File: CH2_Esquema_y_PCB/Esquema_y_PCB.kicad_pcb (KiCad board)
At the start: 2 copper layers, 230 x 106.5 mm, 44 parts, among them Q1 BC547, Q10 BC857, Q2 BC547, Q3 BC547, Q4 BC547, Q5 IRF9Z34N, Q7 BC547, Q9 BC857, U1 TL431LP, U2 LM358

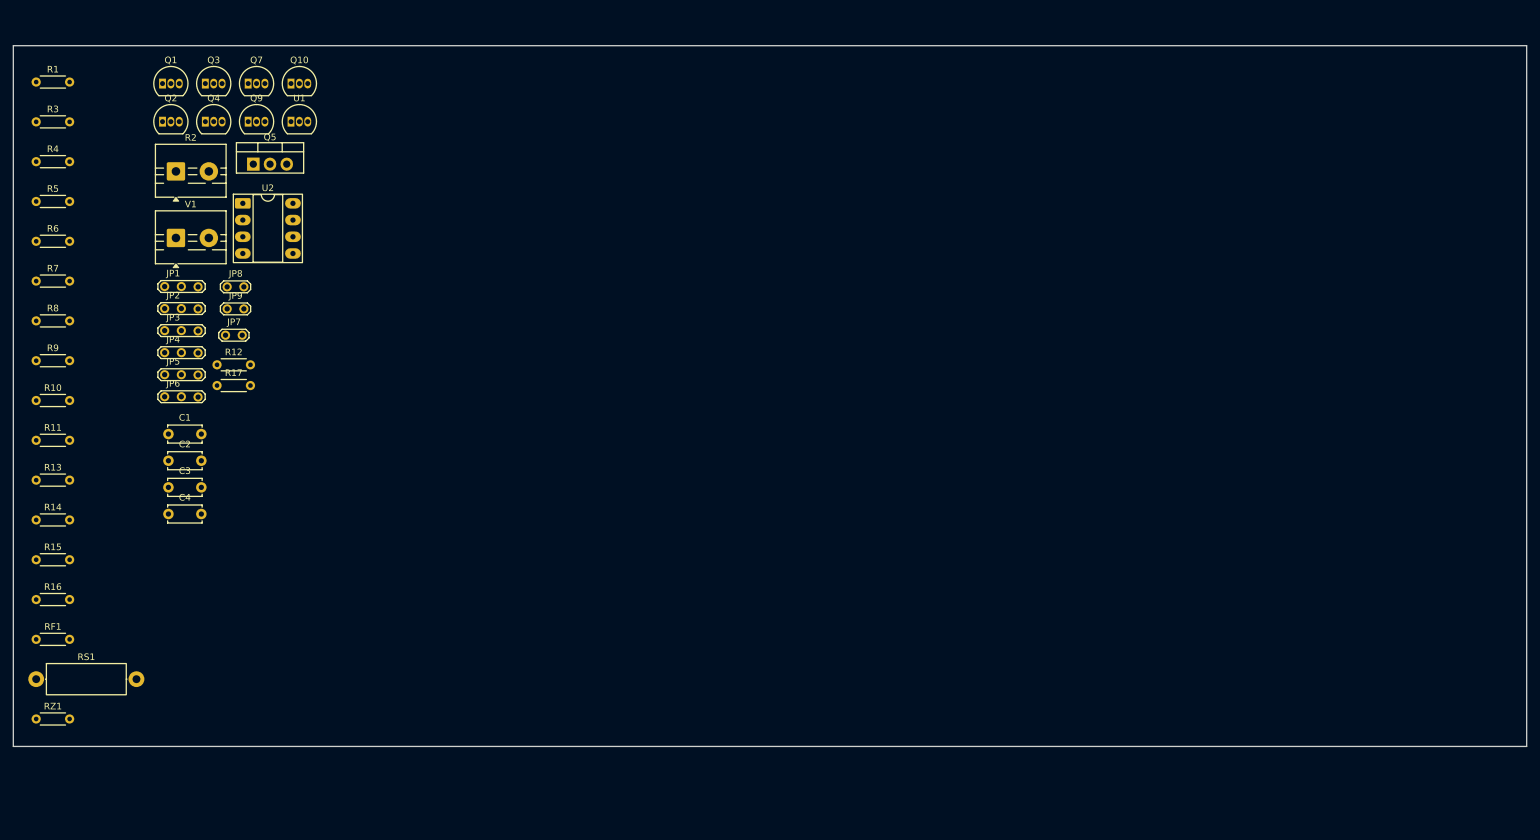
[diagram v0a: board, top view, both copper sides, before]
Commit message: PCB para impresion. Se modifican Jumpers en esquematico
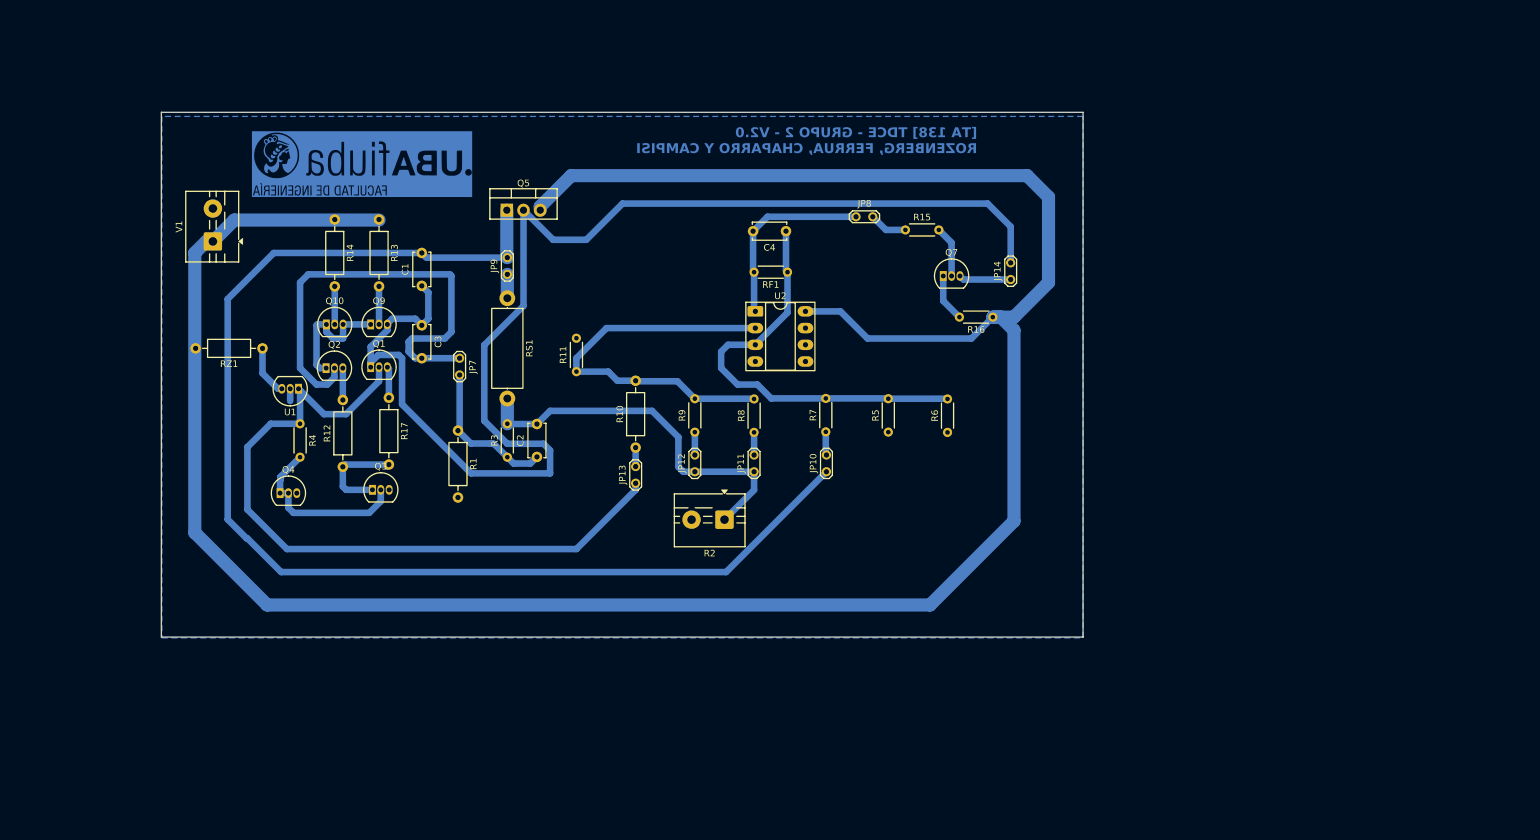
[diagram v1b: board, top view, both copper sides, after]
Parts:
- removed JP1, JP2, JP3, JP4, JP5, JP6: Jumper_3_Bridged12, Jumper_triple:TestPoint_2Pads_Pitch2.54mm_Drill0.8mm
- added G***: LOGO, LOGO, B.Cu at (77.5, 43.0)
- added JP10: Jumper_2_Bridged, TestPoint:TestPoint_2Pads_Pitch2.54mm_Drill0.8mm, F.Cu at (148.1, 89.8)
- added JP11: Jumper_2_Bridged, TestPoint:TestPoint_2Pads_Pitch2.54mm_Drill0.8mm, F.Cu at (137.1, 89.8)
- added JP12: Jumper_2_Bridged, TestPoint:TestPoint_2Pads_Pitch2.54mm_Drill0.8mm, F.Cu at (128.1, 89.8)
- added JP13: Jumper_2_Bridged, TestPoint:TestPoint_2Pads_Pitch2.54mm_Drill0.8mm, F.Cu at (119.1, 91.5)
- added JP14: Jumper_2_Bridged, TestPoint:TestPoint_2Pads_Pitch2.54mm_Drill0.8mm, F.Cu at (176.1, 60.5)
- R1, R10, R12, R13, R14, R17, RZ1: footprint Resistor_THT:R_Axial_DIN0204_L3.6mm_D1.6mm_P5.08mm_Horizontal -> Resistor_THT:R_Axial_DIN0207_L6.3mm_D2.5mm_P10.16mm_Horizontal
- moved R16 151.6 mm to (173.4, 66.2), turned to 180 degrees
- moved R6 141.5 mm to (166.5, 83.8), turned to 90 degrees
- moved R15 141.3 mm to (160.1, 53.0)
- moved R5 134.2 mm to (157.5, 83.7), turned to 90 degrees
- moved RF1 127.1 mm to (142.2, 59.4), turned to 180 degrees
- moved R7 122.2 mm to (148.0, 83.7), turned to 90 degrees
- moved R8 110.4 mm to (137.1, 83.8), turned to 90 degrees
- moved Q7 109.6 mm to (165.8, 60.0)
- moved C4 103.2 mm to (141.9, 53.2), turned to 180 degrees
- moved R9 100.7 mm to (128.1, 83.7), turned to 90 degrees
- moved R2 98.7 mm to (132.6, 97.0), turned to 180 degrees
- moved JP8 96.2 mm to (152.6, 51.0)
- moved RS1 92.1 mm to (99.6, 63.4), turned to -90 degrees
- moved R10 91.4 mm to (119.1, 86.1), turned to 90 degrees
- moved R3 87.9 mm to (99.6, 87.5), turned to 90 degrees
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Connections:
- Q7 pad 3: /gate -> Net-(JP14-A)
- R5 pad 1: Net-(JP1-C) -> GND
- R6 pad 1: Net-(JP2-C) -> GND
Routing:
- net VCC: track 0.00 -> 376.3 mm
- net /gate: track 0.00 -> 195.6 mm
- net /drain: track 0.00 -> 187.1 mm
- net /in: track 0.00 -> 109.0 mm
- net Net-(JP7-A): track 0.00 -> 70.0 mm
- net Net-(U2A-+): track 0.00 -> 64.1 mm
- net Net-(U2A--): track 0.00 -> 59.9 mm
- net /out: track 0.00 -> 57.8 mm
- net Net-(JP8-A): track 0.00 -> 28.9 mm
- net Net-(Q3-B): track 0.00 -> 27.1 mm
- net Net-(JP7-B): track 0.00 -> 23.0 mm
- net Net-(Q10-B): track 0.00 -> 19.6 mm
- net Net-(Q3-C): track 0.00 -> 15.4 mm
- net Net-(JP14-A): track 0.00 -> 7.93 mm
- net Net-(Q7-B): track 0.00 -> 7.80 mm
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- added copper zone on B.Cu, net GND
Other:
- board size 230 x 106.5 mm -> 140.1 x 79.8 mm
- board text added: "[TA 138] TDCE - GRUPO 2 - V2.0 ROZENBERG, FERRUA, CHAPARRO Y CAMPISI"

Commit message: Rehecho PCB
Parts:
- C2, C3: footprint Capacitor_THT:C_Disc_D5.0mm_W2.5mm_P5.00mm -> Capacitor_THT:C_Disc_D7.5mm_W5.0mm_P7.50mm
- Q1, Q10, Q2, Q3, Q4, Q7, Q9, U1: footprint Package_TO_SOT_THT:TO-92_Inline -> Package_TO_SOT_THT:TO-92_Wide
- R11, R15, R16, R3, R4, R5, R6, R7, R8, R9, RF1: footprint Resistor_THT:R_Axial_DIN0204_L3.6mm_D1.6mm_P5.08mm_Horizontal -> Resistor_THT:R_Axial_DIN0207_L6.3mm_D2.5mm_P10.16mm_Horizontal
- RS1: footprint Resistor_THT:R_Axial_DIN0414_L11.9mm_D4.5mm_P15.24mm_Horizontal -> Resistor_THT:R_Axial_Power_L20.0mm_W6.4mm_P25.40mm
- moved G*** 112.4 mm to (169.1, 108.2)
- moved JP10 44.2 mm to (122.1, 54.0), turned to -90 degrees
- moved R16 35.2 mm to (148.0, 41.8), turned to -90 degrees
- moved R7 34.4 mm to (122.1, 61.0), turned to -90 degrees
- moved R11 18.7 mm to (126.5, 65.7)
- moved R6 18.4 mm to (148.8, 89.0)
- moved R5 14.5 mm to (143.9, 88.9)
- moved Q7 14.5 mm to (151.5, 58.3)
- moved V1 14.3 mm to (50.8, 41.0), turned to -90 degrees
- moved RS1 12.6 mm to (109.5, 55.6)
- moved Q10 11.8 mm to (63.7, 59.0), turned to -90 degrees
- moved C3 11.6 mm to (96.5, 61.5)
- moved R15 11.0 mm to (170.5, 49.4), turned to -90 degrees
- moved C2 9.83 mm to (96.8, 80.9), turned to 0 degrees
- moved R1 9.36 mm to (94.2, 92.6)
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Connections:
- Q10 pad 1: Net-(Q10-B) -> Net-(Q10-E)
- Q10 pad 2: Net-(Q10-E) -> Net-(Q10-B)
- Q5 pad 1: /drain -> /gate
- Q5 pad 2: /gate -> /drain
- Q9 pad 1: Net-(Q10-B) -> Net-(Q9-E)
- Q9 pad 2: Net-(Q9-E) -> Net-(Q10-B)
- U2 pad 5: (no net) -> GND
- U2 pad 6: (no net) -> GND
- U2 pad 7: (no net) -> GND
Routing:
- net /drain: track 187.1 -> 55.4 mm
- net /gate: track 195.6 -> 148.4 mm
- net /in: track 109.0 -> 155.4 mm
- net VCC: track 376.3 -> 352.3 mm
- net Net-(JP7-A): track 70.0 -> 47.0 mm
- net Net-(Q10-B): track 19.6 -> 40.9 mm
- net Net-(JP14-A): track 7.93 -> 24.4 mm
- net Net-(U2A--): track 59.9 -> 47.4 mm
- net Net-(Q7-B): track 7.80 -> 18.1 mm
- net Net-(JP8-B): track 5.79 -> 16.0 mm
- net Net-(U2A-+): track 64.1 -> 72.7 mm
- net Net-(Q10-E): track 5.78 -> 10.9 mm
- net Net-(JP8-A): track 28.9 -> 33.1 mm
- net Net-(JP7-B): track 23.0 -> 27.3 mm
- net Net-(Q3-C): track 15.4 -> 11.4 mm
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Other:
- board size 140.1 x 79.8 mm -> 143.4 x 79.8 mm

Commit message: Reversion del PCB
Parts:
- R16, R7: footprint Resistor_THT:R_Axial_DIN0207_L6.3mm_D2.5mm_P10.16mm_Horizontal -> Resistor_THT:R_Axial_DIN0207_L6.3mm_D2.5mm_P15.24mm_Horizontal
- moved JP13 47.6 mm to (143.7, 132.3)
- moved R10 45.8 mm to (143.8, 124.8)
- moved R11 45.2 mm to (152.0, 103.0)
- moved R9 44.7 mm to (152.9, 123.3)
- moved R2 44.5 mm to (155.7, 134.5)
- moved JP12 44.4 mm to (153.1, 128.7)
- moved JP14 43.7 mm to (203.7, 96.8), turned to 90 degrees
- moved R15 43.7 mm to (195.8, 85.0)
- moved U2 42.5 mm to (162.8, 99.3)
- moved JP11 42.1 mm to (161.2, 129.8)
- moved R8 42.1 mm to (161.5, 123.3)
- moved C4 41.9 mm to (165.4, 85.7)
- moved R6 41.4 mm to (173.7, 122.1)
- moved R5 41.4 mm to (168.9, 121.9)
- moved RF1 41.2 mm to (170.4, 89.3)
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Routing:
- net GND: track 0.00 -> 31.9 mm
- net VCC: track 352.3 -> 336.4 mm
- net /gate: track 148.4 -> 160.0 mm
- net Net-(Q9-E): track 5.76 -> 12.8 mm
- net /out: track 61.1 -> 55.2 mm
- net Net-(Q7-C): track 9.15 -> 4.75 mm
- net /in: track 155.4 -> 158.8 mm
- net Net-(U2A-+): track 72.7 -> 75.8 mm
- net Net-(U2A--): track 47.4 -> 49.9 mm
- net Net-(JP13-B): track 2.88 -> 5.27 mm
- net Net-(JP8-A): track 33.1 -> 34.9 mm
- net Net-(Q10-E): track 10.9 -> 12.5 mm
- net /drain: track 55.4 -> 53.9 mm
- net Net-(Q7-B): track 18.1 -> 19.4 mm
- net Net-(JP10-B): track 4.43 -> 3.13 mm
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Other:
- board size 143.4 x 79.8 mm -> 143.4 x 83.7 mm
- board text added: "Disipador"
- board text added: "[ T A 1 3 8 ] T D C E - G R U P O 2 - V 3 . 0 R O Z E N B E R G , F E R R U A , C H A P A R R O Y C A M P I S I"
- board text removed: "[TA 138] TDCE - GRUPO 2 - V2.0 ROZENBERG, FERRUA, CHAPARRO Y CAMPISI"
